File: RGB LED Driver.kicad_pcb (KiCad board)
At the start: 2 copper layers, 108 x 44.4 mm, 39 parts, among them J1 UART, J2 LED_STRIP_OUTPUT, J3 5V_POWER_INPUT, J4 PWR_BTN, J5 LED_STRIP_OUTPUT1, J6 LED_STRIP_OUTPUT2, SW1 SW_Push, SW2 SW_Push, SW3 SW_Push, U1 ESP-12E, U2 AMS1117-3.3, U3 74LVC2G17, U4 74LVC2G17

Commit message: PCB done, and ready for feedback
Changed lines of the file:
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@@
     (thickness 1.6)
     (drawings 11)
-    (tracks 361)
+    (tracks 362)
     (zones 0)
     (modules 39)
@@
   (segment (start 149.52 70.19) (end 149.86 69.85) (width 0.25) (layer F.Cu) (net 3))
   (segment (start 140.99 70.19) (end 149.52 70.19) (width 0.25) (layer F.Cu) (net 3))
-  (segment (start 139.829997 57.364999) (end 142.454999 57.364999) (width 0.25) (layer F.Cu) (net 3))
-  (segment (start 137.81501 55.350012) (end 139.829997 57.364999) (width 0.25) (layer F.Cu) (net 3))
-  (segment (start 137.81501 53.72501) (end 137.81501 55.350012) (width 0.25) (layer F.Cu) (net 3))
-  (segment (start 134.89 50.8) (end 137.81501 53.72501) (width 0.25) (layer F.Cu) (net 3))
-  (segment (start 142.454999 57.364999) (end 144.78 59.69) (width 0.25) (layer F.Cu) (net 3))
   (segment (start 144.78 59.69) (end 144.78 59.69) (width 0.25) (layer F.Cu) (net 3))
   (via (at 144.78 59.69) (size 0.8) (drill 0.4) (layers F.Cu B.Cu) (net 3))
@@
   (segment (start 144.78 67.9) (end 144.78 64.77) (width 0.25) (layer F.Cu) (net 3))
   (segment (start 140.99 70.19) (end 142.49 70.19) (width 0.25) (layer F.Cu) (net 3))
+  (segment (start 134.89 50.8) (end 134.89 51.07) (width 0.25) (layer F.Cu) (net 3))
+  (segment (start 139.829997 57.364999) (end 142.454999 57.364999) (width 0.25) (layer F.Cu) (net 3))
+  (segment (start 142.454999 57.364999) (end 144.78 59.69) (width 0.25) (layer F.Cu) (net 3))
+  (segment (start 139.414999 55.594999) (end 139.414999 56.950001) (width 0.25) (layer F.Cu) (net 3))
+  (segment (start 139.414999 56.950001) (end 139.829997 57.364999) (width 0.25) (layer F.Cu) (net 3))
+  (segment (start 134.89 51.07) (end 139.414999 55.594999) (width 0.25) (layer F.Cu) (net 3))
   (segment (start 121.28 66.04) (end 123.19 67.95) (width 0.25) (layer F.Cu) (net 4))
   (segment (start 120.65 66.04) (end 121.28 66.04) (width 0.25) (layer F.Cu) (net 4))

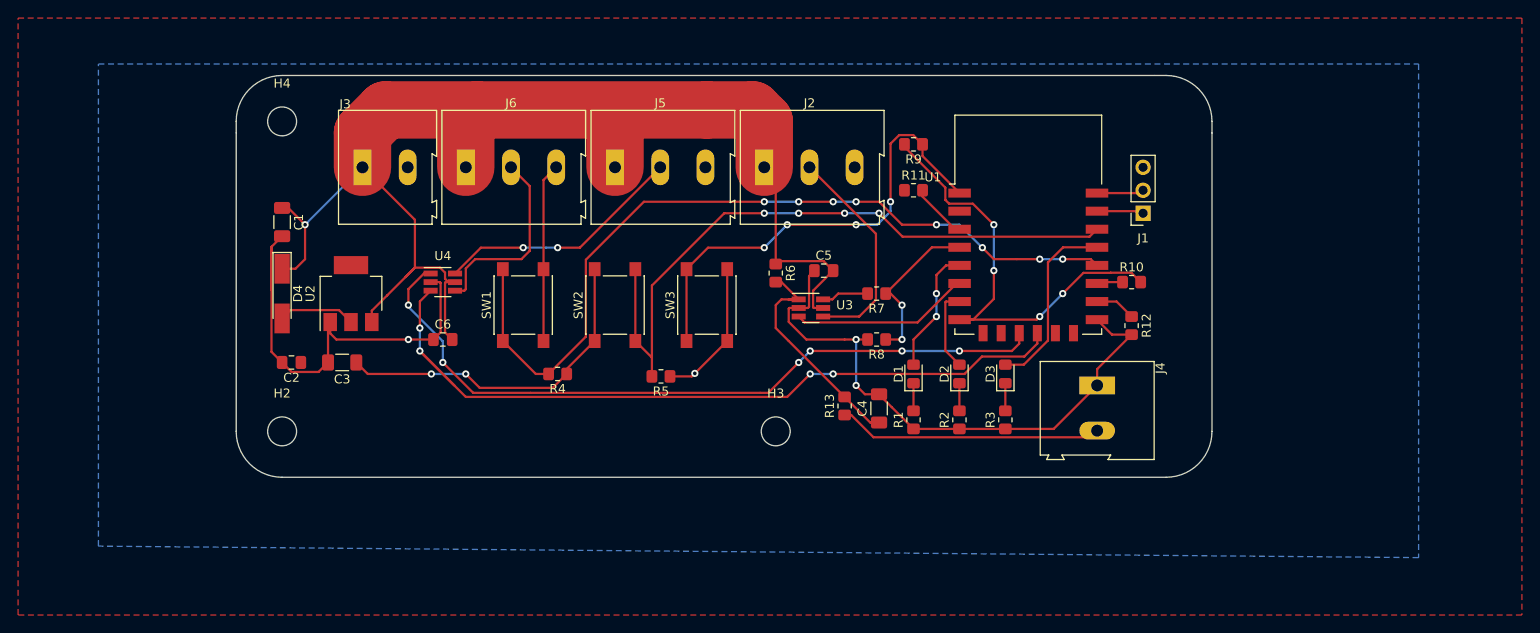
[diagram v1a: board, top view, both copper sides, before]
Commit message: PCB updated and fixed problems
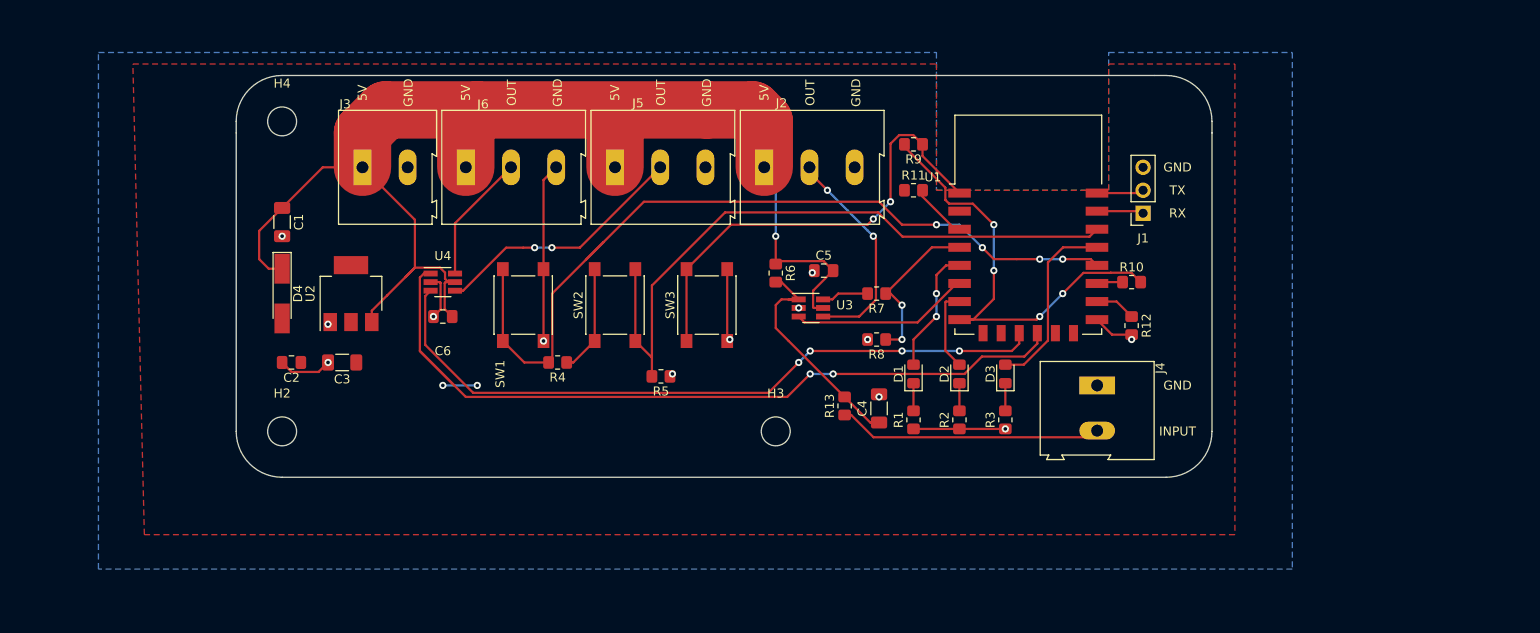
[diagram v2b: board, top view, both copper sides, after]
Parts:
- J2: value LED_STRIP_OUTPUT -> LED_STRIP_OUTPUT0
- moved C6 2.54 mm to (83.8, 69.8)
- moved R4 1.27 mm to (96.5, 74.9)
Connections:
- U4 pad 1: Net-(U1-Pad11) -> Net-(U1-Pad12)
- U4 pad 3: Net-(U1-Pad12) -> Net-(U1-Pad11)
- U4 pad 4: Net-(J6-Pad2) -> Net-(J5-Pad2)
- U4 pad 6: Net-(J5-Pad2) -> Net-(J6-Pad2)
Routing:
- net GND: track 152.5 -> 54.8 mm, vias 4 -> 13
- net +3V3: track 96.6 -> 66.5 mm
- net Net-(J6-Pad2): track 21.5 -> 14.3 mm
- net Net-(U1-Pad11): track 81.2 -> 77.7 mm, vias 6 -> 4
- net Net-(U1-Pad12): track 86.7 -> 88.9 mm, vias 4 -> 2
- net +5V: track 151.3 -> 153.0 mm
- net /FLASH_BTN: track 91.0 -> 92.0 mm, vias 8 -> 4
- net Net-(J5-Pad2): track 27.6 -> 28.4 mm
- net /RESET: track 52.5 -> 51.9 mm, vias 4 -> 2
- net Net-(J2-Pad2): track 24.3 -> 24.9 mm, vias 0 -> 2
- net /MEM_RST: vias 4 -> 0
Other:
- board text added: "5V"
- board text added: "GND"
- board text added: "INPUT"
- board text added: "OUT"
- board text added: "RX"
- board text added: "TX"

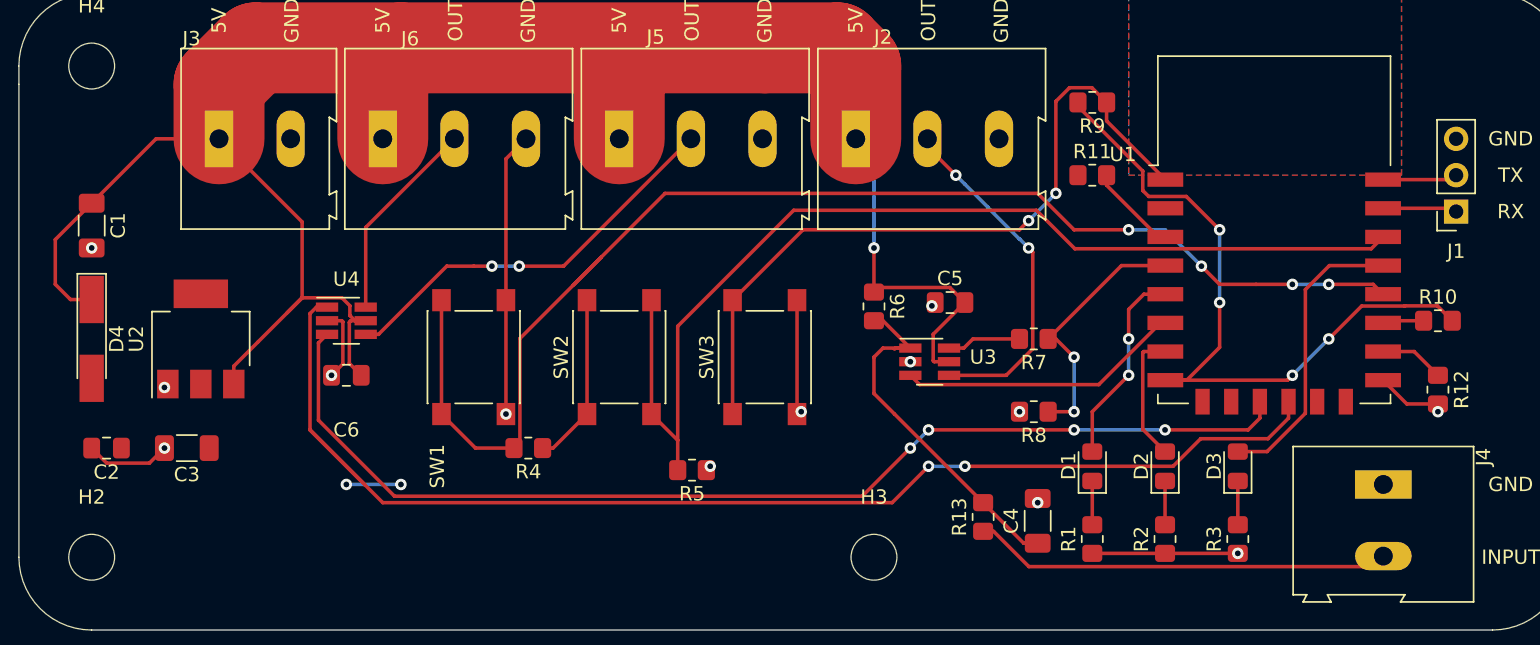
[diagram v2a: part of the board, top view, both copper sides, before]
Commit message: PCB updated, and repaired problem with via on pads
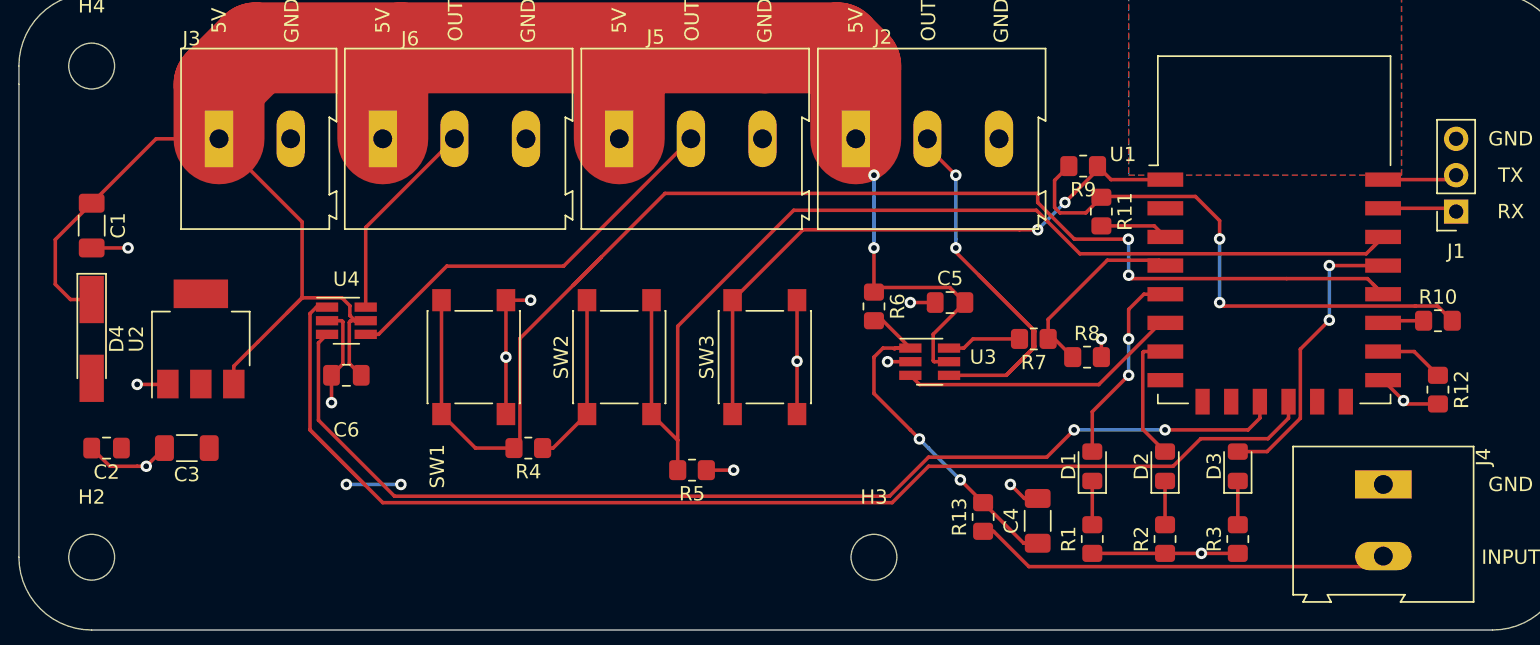
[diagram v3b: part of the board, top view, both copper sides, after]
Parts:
- moved R8 5.32 mm to (135.5, 68.6), turned to 0 degrees
- moved R9 4.49 mm to (135.3, 55.2)
- moved R11 2.62 mm to (136.5, 58.4), turned to 270 degrees
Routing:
- net +3V3: track 66.5 -> 56.5 mm, vias 6 -> 4
- net Net-(J2-Pad2): track 24.9 -> 34.0 mm
- net /RESET: track 51.9 -> 43.0 mm
- net GND: track 54.8 -> 60.3 mm, vias 13 -> 14
- net /PWR_BTN: track 18.3 -> 13.7 mm, vias 2 -> 0
- net +5V: track 153.0 -> 149.9 mm, vias 1 -> 2
- net /FLASH_BTN: track 92.0 -> 94.8 mm, vias 4 -> 2
- net /MEM_RST: track 74.6 -> 76.1 mm
- net Net-(R11-Pad2): track 6.30 -> 5.27 mm
- net Net-(U1-Pad12): vias 2 -> 0
- net Net-(C4-Pad1): vias 0 -> 2
- net Net-(U1-Pad11): vias 4 -> 2
- net Net-(J5-Pad2): vias 2 -> 0
- net /STATE_LED3: vias 0 -> 2

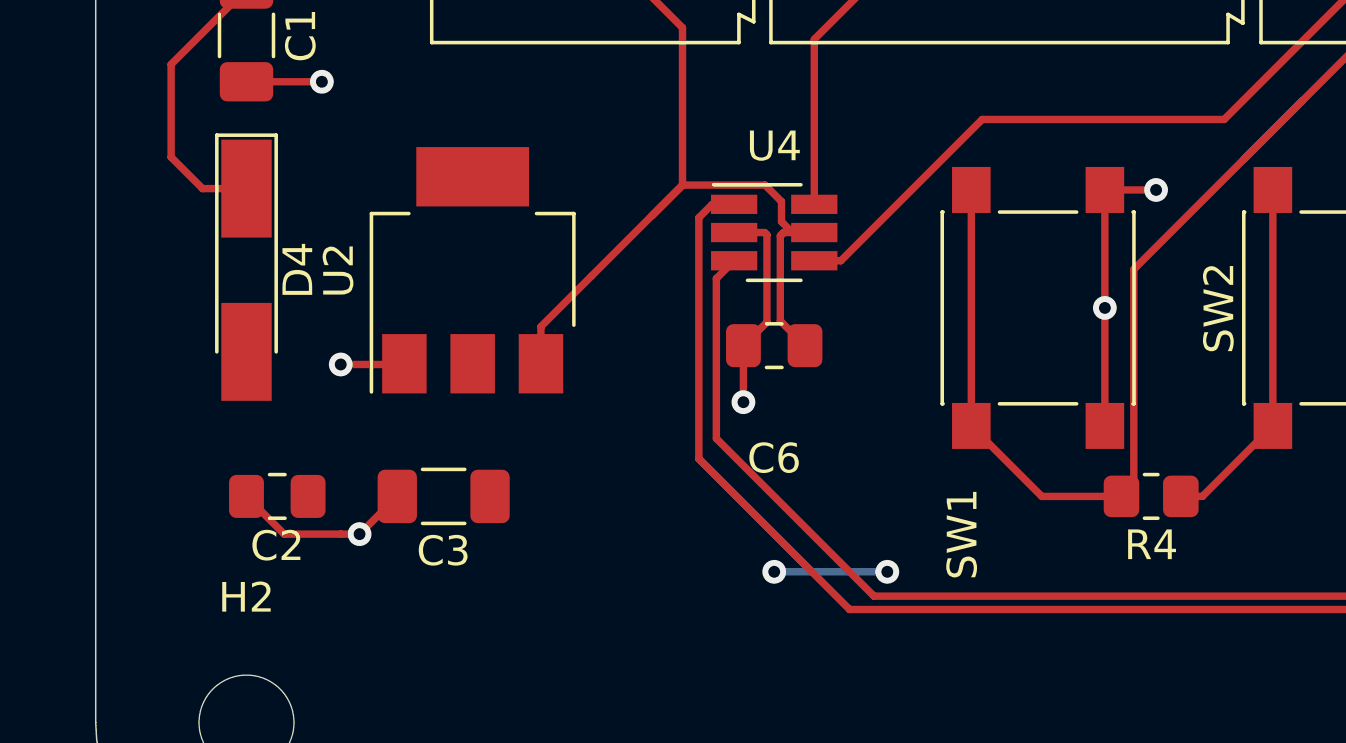
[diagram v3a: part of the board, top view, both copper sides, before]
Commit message: PCB updated, and repaired problem with via on pads
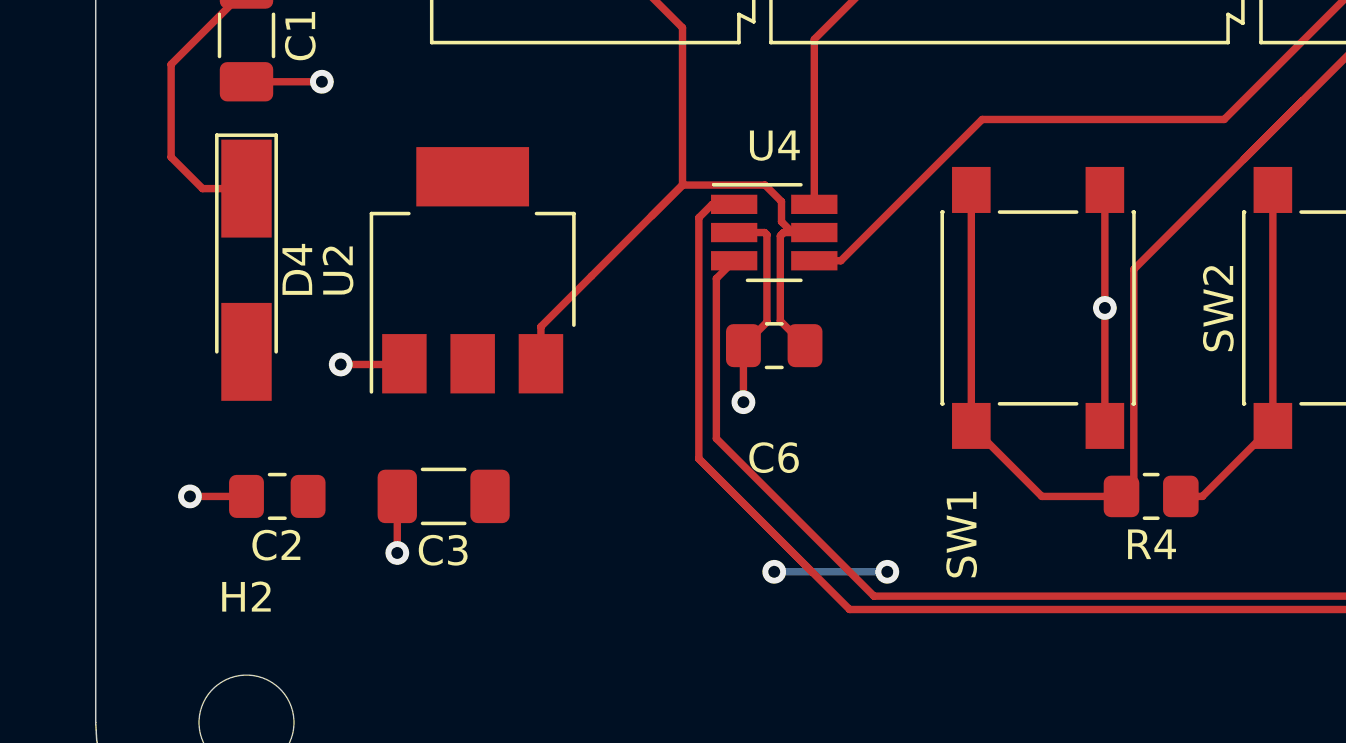
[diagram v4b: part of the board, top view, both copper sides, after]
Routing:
- net GND: track 60.3 -> 56.2 mm
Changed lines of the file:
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@@
     (thickness 1.6)
     (drawings 27)
-    (tracks 317)
+    (tracks 315)
     (zones 0)
     (modules 39)
@@
   (segment (start 71.12 70.7) (end 71.12 70.7) (width 0.25) (layer F.Cu) (net 1))
   (segment (start 71.12 74.93) (end 71.12 74.93) (width 0.25) (layer F.Cu) (net 1))
-  (via (at 69.85 76.2) (size 0.8) (drill 0.4) (layers F.Cu B.Cu) (net 1))
   (segment (start 71.12 70.7) (end 71.36 70.46) (width 0.25) (layer F.Cu) (net 1))
   (via (at 69.215 70.485) (size 0.8) (drill 0.4) (layers F.Cu B.Cu) (net 1))
@@
   (segment (start 71.335 70.485) (end 71.36 70.46) (width 0.25) (layer F.Cu) (net 1))
   (segment (start 69.215 70.485) (end 71.335 70.485) (width 0.25) (layer F.Cu) (net 1))
-  (segment (start 71.12 74.93) (end 69.85 76.2) (width 0.25) (layer F.Cu) (net 1))
-  (segment (start 69.85 76.2) (end 69.215 76.2) (width 0.25) (layer F.Cu) (net 1))
-  (segment (start 67.31 76.2) (end 69.215 76.2) (width 0.25) (layer F.Cu) (net 1))
-  (segment (start 66.04 74.93) (end 67.31 76.2) (width 0.25) (layer F.Cu) (net 1))
   (segment (start 68.58 60.96) (end 66.04 60.96) (width 0.25) (layer F.Cu) (net 1))
   (segment (start 115.28 68.87) (end 115.28 72.555) (width 0.25) (layer F.Cu) (net 1))
@@
   (via (at 157.6175 71.6175) (size 0.8) (drill 0.4) (layers F.Cu B.Cu) (net 1))
   (segment (start 82.7825 71.755) (end 82.7825 69.85) (width 0.25) (layer F.Cu) (net 1))
-  (segment (start 94.96 64.605) (end 96.685 64.605) (width 0.25) (layer F.Cu) (net 1))
-  (segment (start 96.685 64.605) (end 96.685 64.605) (width 0.25) (layer F.Cu) (net 1))
-  (via (at 96.685 64.605) (size 0.8) (drill 0.4) (layers F.Cu B.Cu) (net 1))
   (segment (start 136.525 68.58) (end 136.525 67.31) (width 0.25) (layer F.Cu) (net 1))
   (segment (start 136.525 67.31) (end 136.525 67.31) (width 0.25) (layer F.Cu) (net 1))
@@
   (segment (start 110.855 76.47) (end 110.855 76.47) (width 0.25) (layer F.Cu) (net 1))
   (via (at 110.855 76.47) (size 0.8) (drill 0.4) (layers F.Cu B.Cu) (net 1))
+  (segment (start 71.12 74.93) (end 71.12 76.835) (width 0.25) (layer F.Cu) (net 1))
+  (segment (start 71.12 76.835) (end 71.12 76.835) (width 0.25) (layer F.Cu) (net 1))
+  (via (at 71.12 76.835) (size 0.8) (drill 0.4) (layers F.Cu B.Cu) (net 1))
+  (segment (start 66.04 74.93) (end 64.135 74.93) (width 0.25) (layer F.Cu) (net 1))
+  (segment (start 64.135 74.93) (end 64.135 74.93) (width 0.25) (layer F.Cu) (net 1))
+  (via (at 64.135 74.93) (size 0.8) (drill 0.4) (layers F.Cu B.Cu) (net 1))
   (segment (start 84.064999 66.115001) (end 84.14 66.04) (width 0.25) (layer F.Cu) (net 2))
   (segment (start 75.96 70.424998) (end 75.96 70.46) (width 0.25) (layer F.Cu) (net 2))
